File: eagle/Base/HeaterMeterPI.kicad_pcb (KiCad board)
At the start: 2 copper layers, 94.6 x 46.1 mm, 66 parts, among them IC1 OKI-78SR-5, IC2 ATmega328P, IC4 MCP1700, IC5 AD8495, J1 RPi, J2 PROBE, J4 PCC-SMP, J9 Barrel_Jack_Switch, Q1 BS170, Q2 BS170, Q3 FQU11P06TU, Q5 BS170, Y1 16MHz

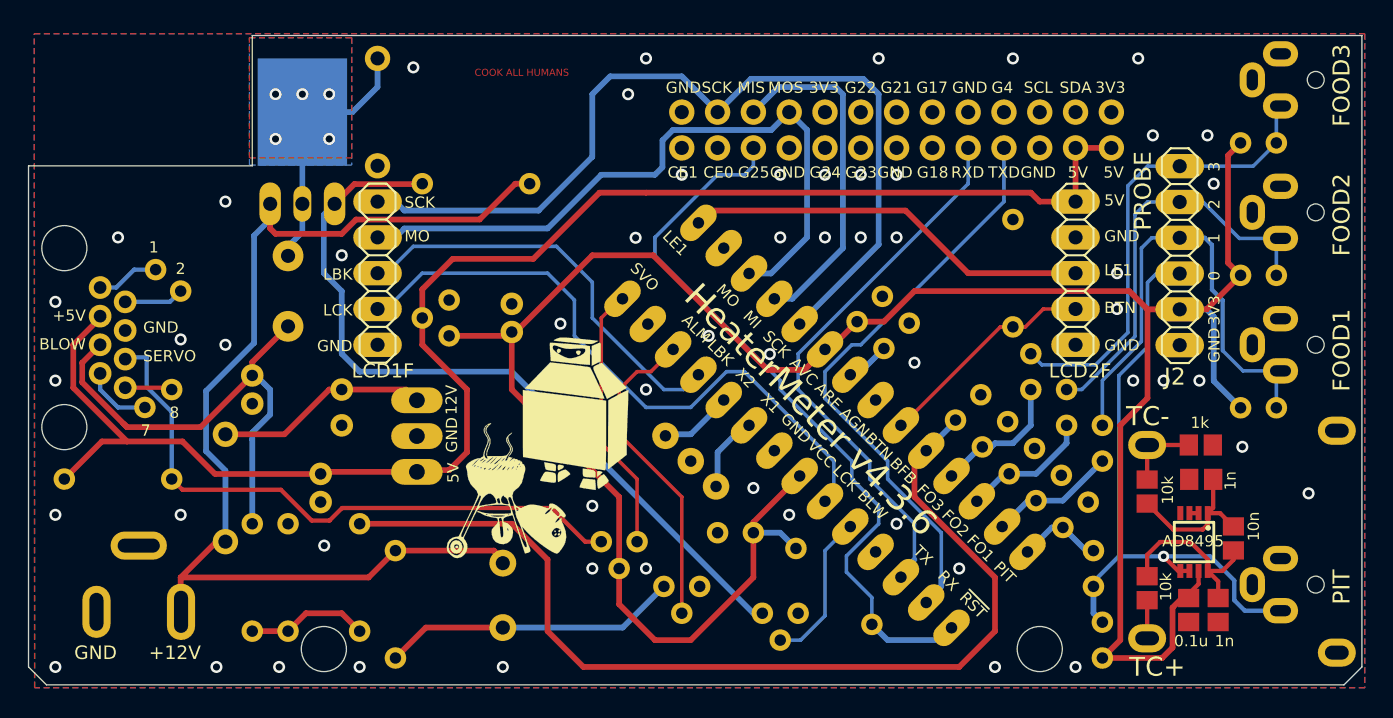
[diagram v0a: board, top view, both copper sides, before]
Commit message: [eagle] Upgraded to KiCad 8.0. Moved to 2.5A fan drive solution.
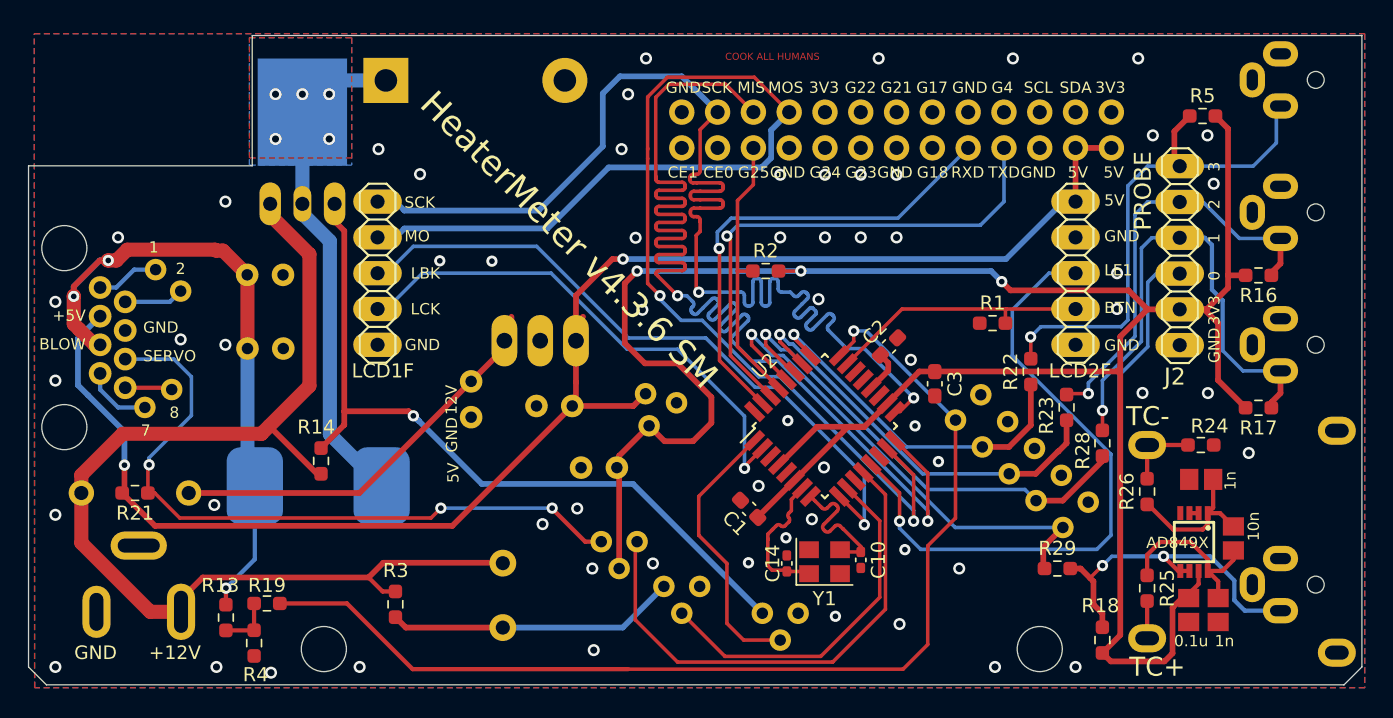
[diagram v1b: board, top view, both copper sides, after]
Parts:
- removed G***: LOGO, HeaterMeterPI:boxy
- removed IC2: ATmega328P, HeaterMeterPI:DIL28-3
- removed R20: 10k, HeaterMeterPI:0204_7
- added C10: 22pF, Capacitor_SMD:C_0402_1005Metric_Pad0.74x0.62mm_HandSolder, F.Cu at (160.2, 119.0)
- added C14: 22pF, Capacitor_SMD:C_0402_1005Metric_Pad0.74x0.62mm_HandSolder, F.Cu at (155.0, 119.2)
- added C19: 47u/25, HeaterMeterPI:E2,5-5, B.Cu at (118.0, 104.0)
- added R2: 10k, Resistor_SMD:R_0603_1608Metric_Pad0.98x0.95mm_HandSolder, F.Cu at (153.5, 98.5)
- added U2: ATmega328P-A, Package_QFP:TQFP-32_7x7mm_P0.8mm, F.Cu at (157.7, 109.5)
- C1, C2, C3: footprint HeaterMeterPI:C025-025X050 -> Capacitor_SMD:C_0603_1608Metric_Pad1.08x0.95mm_HandSolder; moved to F.Cu
- C12, C5, C6: footprint HeaterMeterPI:E2-5 -> HeaterMeterPI:E2,5-5
- D2: footprint HeaterMeterPI:DO41-7 -> Diode_THT:D_DO-201AD_P12.70mm_Horizontal
- IC5: value AD8495 -> AD849X
- L1: footprint HeaterMeterPI:E5-9 -> HeaterMeterPI:MSS1278T
- R1, R13, R14, R19, R21, R3, R4: footprint HeaterMeterPI:0204_7 -> Resistor_SMD:R_0603_1608Metric_Pad0.98x0.95mm_HandSolder; moved to F.Cu
- R16, R17, R18, R22, R23, R28, R29, R5: footprint HeaterMeterPI:0207_2V -> Resistor_SMD:R_0603_1608Metric_Pad0.98x0.95mm_HandSolder; moved to F.Cu
- R24, R25, R26: footprint HeaterMeterPI:R0805 -> Resistor_SMD:R_0603_1608Metric_Pad0.98x0.95mm_HandSolder
- Y1: footprint HeaterMeterPI:RESONATOR-PTH -> Crystal:Crystal_SMD_3225-4Pin_3.2x2.5mm; moved to F.Cu
- moved R14 22.5 mm to (122.0, 112.0), turned to 90 degrees
- moved L1 20.2 mm to (115.8, 119.8), turned to 90 degrees
- moved C5 17.6 mm to (138.5, 108.1), turned to 180 degrees
- moved IC4 16.6 mm to (146.2, 108.7), turned to -140 degrees
- moved IC1 12.4 mm to (137.5, 98.4), turned to 180 degrees
- moved C6 12.3 mm to (141.7, 112.5), turned to 180 degrees
- moved Y1 11.9 mm to (157.7, 119.1), turned to 0 degrees
- moved C4 9.20 mm to (132.6, 107.6)
- moved C12 8.19 mm to (118.0, 98.8), turned to 0 degrees
- moved C3 7.03 mm to (165.5, 106.5), turned to -90 degrees
- moved R19 6.83 mm to (118.1, 122.1), turned to 0 degrees
- moved D3 6.42 mm to (108.8, 114.2), turned to 180 degrees
- moved R4 5.24 mm to (117.2, 124.9), turned to -90 degrees
- moved R5 4.40 mm to (184.5, 87.5), turned to 0 degrees
- moved R1 3.83 mm to (169.6, 102.2), turned to 0 degrees
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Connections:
- IC5 pad 4: Net-(IC5-Pad4) -> unconnected-(IC5-NC-Pad4)
- J1 pad 10: Net-(J1-Pad10) -> unconnected-(J1-Pad10)
- J1 pad 11: Net-(J1-Pad11) -> unconnected-(J1-Pad11)
- J1 pad 12: Net-(J1-Pad12) -> unconnected-(J1-Pad12)
- J1 pad 13: Net-(J1-Pad13) -> unconnected-(J1-Pad13)
- J1 pad 15: Net-(J1-Pad15) -> unconnected-(J1-Pad15)
- J1 pad 16: Net-(J1-Pad16) -> unconnected-(J1-Pad16)
- J1 pad 19: Net-(J1-Pad19) -> unconnected-(J1-Pad19)
- J1 pad 2: Net-(J1-Pad2) -> unconnected-(J1-Pad2)
- J1 pad 21: Net-(J1-Pad21) -> unconnected-(J1-Pad21)
- J1 pad 23: Net-(J1-Pad23) -> unconnected-(J1-Pad23)
- J1 pad 25: Net-(J1-Pad25) -> unconnected-(J1-Pad25)
- J1 pad 4: Net-(J1-Pad4) -> unconnected-(J1-Pad4)
- J1 pad 6: /~RESET -> /~{RESET}
- J1 pad 9: Net-(J1-Pad9) -> unconnected-(J1-Pad9)
- JP3 pad 3: Net-(JP3-Pad3) -> unconnected-(JP3-Pad3)
- JP4 pad 3: Net-(JP4-Pad3) -> unconnected-(JP4-Pad3)
- JP5 pad 3: Net-(JP5-Pad3) -> unconnected-(JP5-Pad3)
- JP6 pad 3: Net-(JP6-Pad3) -> unconnected-(JP6-Pad3)
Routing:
- net /MISO: track 24.6 -> 87.3 mm, vias 0 -> 2
- net /~RESET: track 52.6 -> 0.00 mm
- net /MOSI: track 48.6 -> 90.0 mm, vias 0 -> 2
- net /PIT: track 6.08 -> 35.4 mm, vias 0 -> 1
- net /FOOD1: track 9.04 -> 33.7 mm, vias 0 -> 1
- net /SCK: track 63.5 -> 86.7 mm, vias 0 -> 2
- net /FOOD2: track 9.34 -> 29.7 mm, vias 0 -> 1
- net /~{RESET}: track 0.00 -> 19.8 mm
- net /LCD_BKLT: track 29.7 -> 47.7 mm, vias 0 -> 1
- net /SERVO: track 19.0 -> 36.3 mm
- net Net-(D2-PadC): track 18.7 -> 35.7 mm
- net /LED1: track 29.1 -> 45.8 mm, vias 0 -> 1
- net /FOOD3: track 9.65 -> 25.6 mm, vias 0 -> 1
- net Net-(IC1-VI): track 15.2 -> 29.1 mm
- net /+12V_BLW: track 35.2 -> 47.8 mm, vias 0 -> 3
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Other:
- net class Default removed
- board text added: "HeaterMeter v4.3.6 SM"
- board text removed: "AGN"
- board text removed: "ALM"
- board text removed: "ARE"
- board text removed: "AVC"
- board text removed: "BFB"
- board text removed: "BLW"
- board text removed: "FO1"
- board text removed: "FO2"
- board text removed: "FO3"
- board text removed: "HeaterMeter v4.3.6"
- board text removed: "MI"
- board text removed: "PIT"
- board text removed: "RX"
- board text removed: "SVO"
- board text removed: "TX"
- board text removed: "VCC"
- board text removed: "X1"
- board text removed: "X2"
- board text removed: "~RST"
